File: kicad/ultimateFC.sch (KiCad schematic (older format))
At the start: 195 parts, among them J1 USB_B_Micro, J2 10132797-011100LF, J3 10132797-011100LF, J4 10132797-011100LF, J5 10132797-011100LF, J6 10132797-011100LF, Q1 DMP2066LSN-7, U1 EFM8BB21F16G-C-QFN20R, U10 NCP81253MNTBG, U11 SiZ200DT, U12 NCP81253MNTBG, U13 SiZ200DT, U14 TPS62824ADMQ, U15 SiZ200DT, U16 NCP81253MNTBG, U17 NCP81253MNTBG, U18 NCP81253MNTBG, U19 NCP81253MNTBG, U2 EFM8BB21F16G-C-QFN20R, U20 SiZ200DT, U21 SiZ200DT, U22 SiZ200DT, U23 SiZ200DT, U24 EFM8BB21F16G-C-QFN20R, U25 NCP81253MNTBG, U26 SiZ200DT, U27 NCP81253MNTBG, U28 NCP81253MNTBG, U29 SiZ200DT, U3 NCP81253MNTBG, U30 SiZ200DT, U31 INA186, U32 LMR33630CQRNX, U33 STM32F745VGHx, U34 AB7456, U35 ZOE-M8Q_ZOE-M8Q, U36 ICM-20602, U37 S25FL064L, U39 BMP280, U4 SiZ200DT, U5 TPS630701, U6 EFM8BB21F16G-C-QFN20R, U7 NCP81253MNTBG, U8 SiZ200DT, U9 NCP81253MNTBG, X1 Molex_734120110, Y1 CSTNE8M00G550000R0, Y2 ECS-270-8-47Q-CES-TR

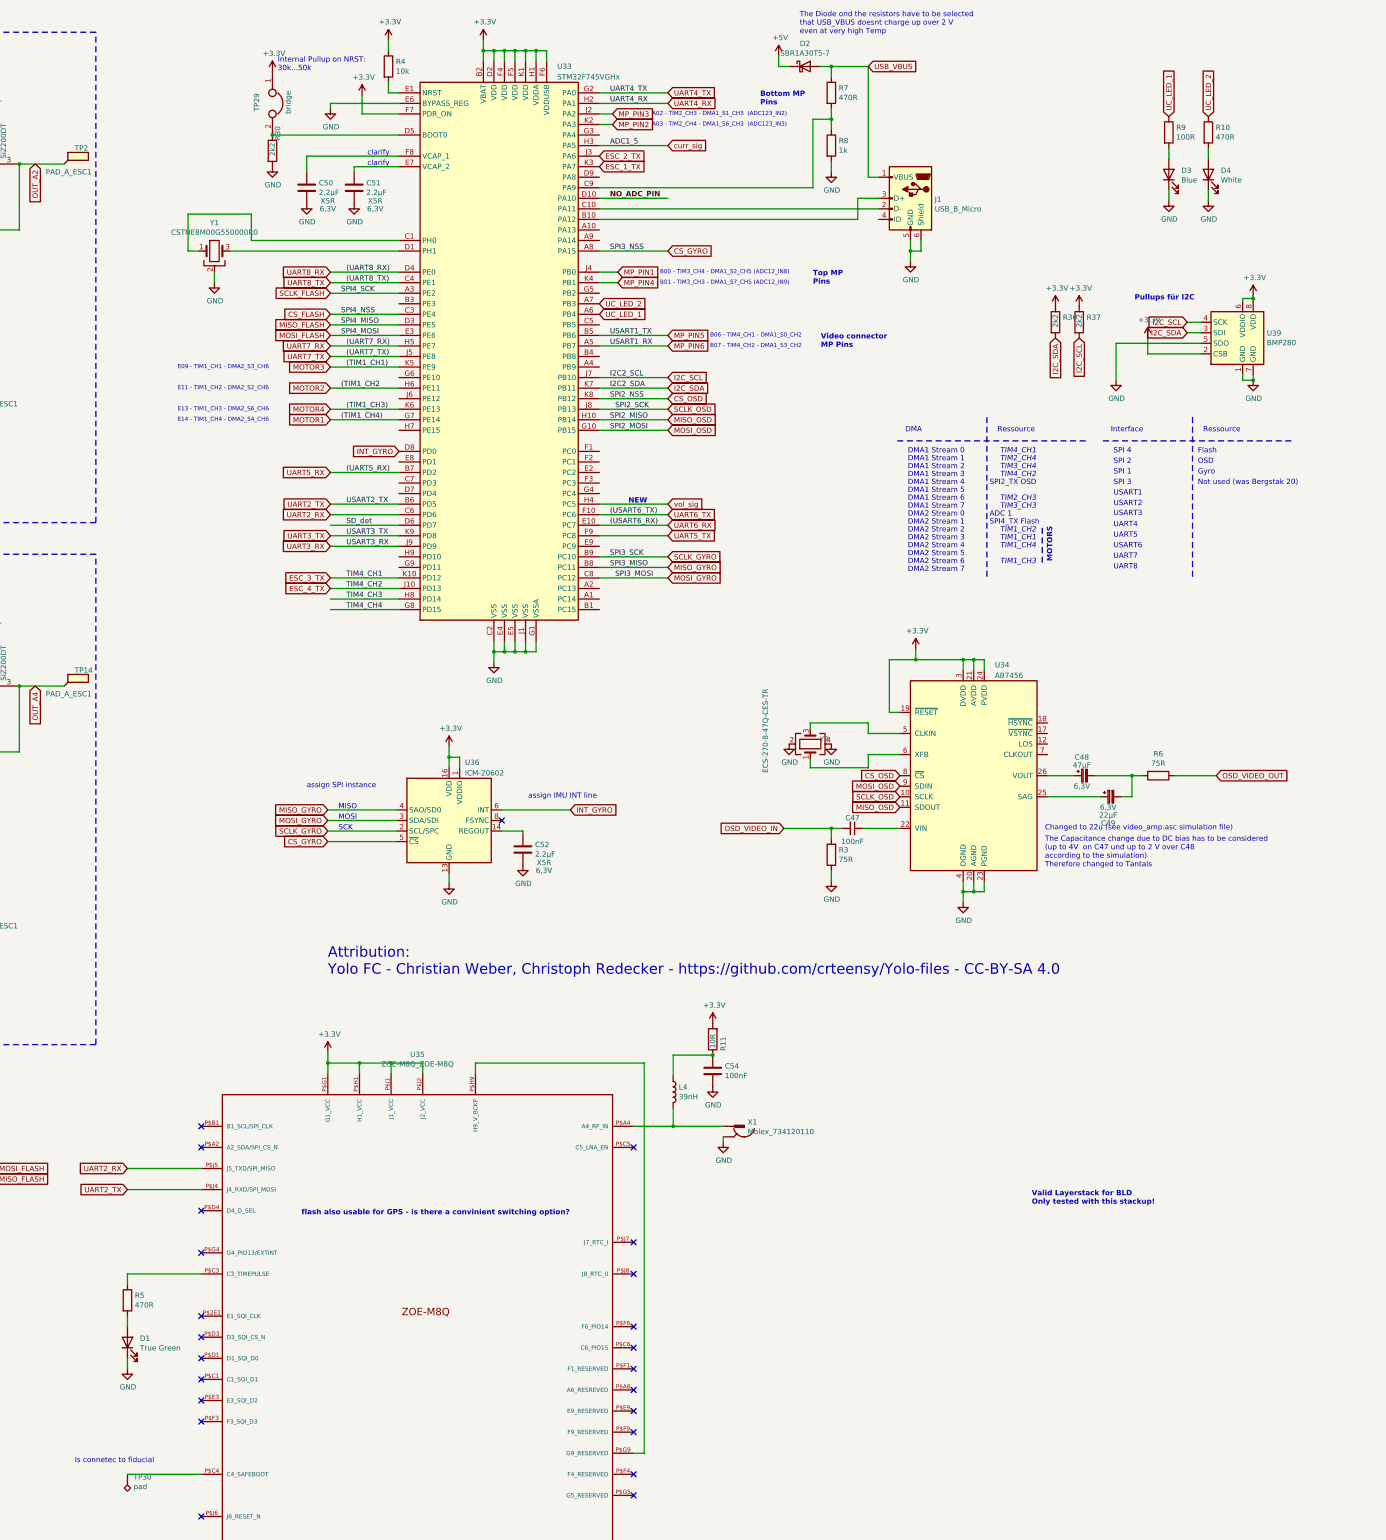
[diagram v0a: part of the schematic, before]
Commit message: exported gerbers and p+p files, started whoop mount adapter
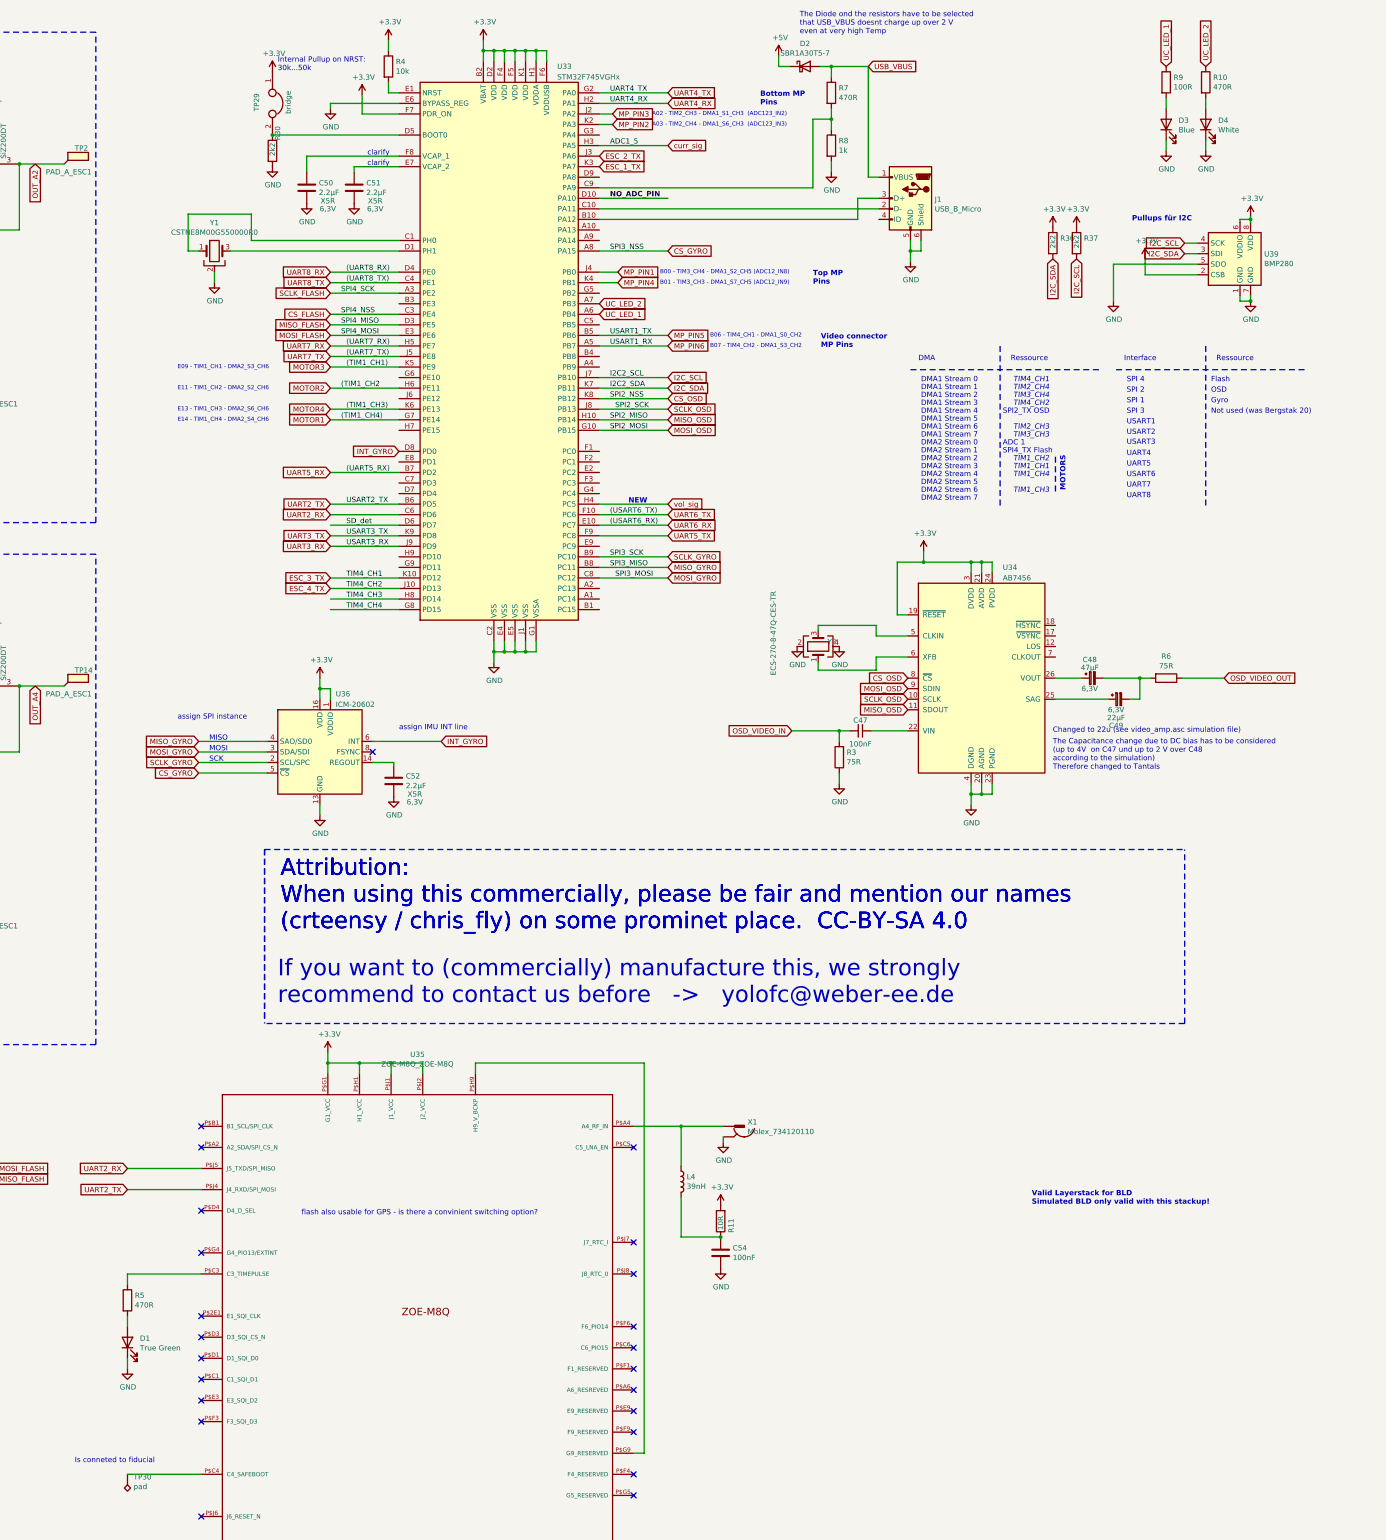
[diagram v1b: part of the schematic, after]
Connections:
- net at U35.P$A4 (A4_RF_IN), X1.1: now also L4.1; no longer L4.2
- net at C54.1, R11.1: now also L4.2; no longer L4.1
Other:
- note added: "Attribution:\nWhen using this commercially, please be fair and mention our names \n(crteensy / chris_fly) on some prominet place. CC-BY-SA 4.0"
- note added: "If you want to (commercially) manufacture this, we strongly \nrecommend to contact us before -> yolofc@weber-ee.de"
- note added: "Is conneted to fiducial"
- note added: "Valid Layerstack for BLD\nSimulated BLD only valid with this stackup!"
- note removed: "Attribution:\nYolo FC - Christian Weber, Christoph Redecker - https://github.com/crteensy/Yolo-files - CC-BY-SA 4.0"
- note removed: "Is connetec to fiducial"
- note removed: "Valid Layerstack for BLD\nOnly tested with this stackup!"
- moved on the sheet: C47, C48, C49, C52, C54, D3, D4, L4, R10, R11, R3, R36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

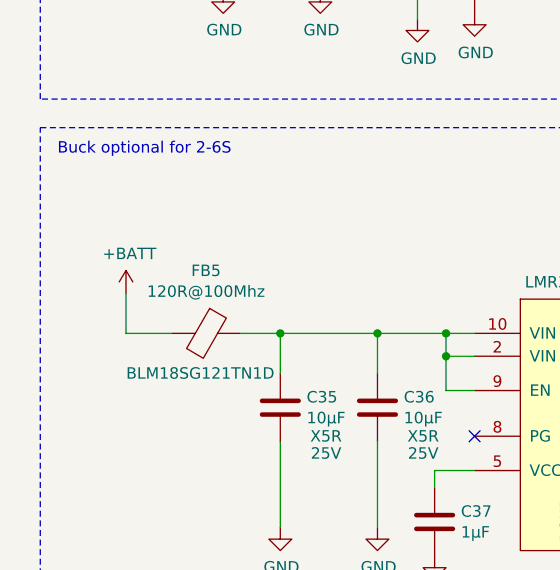
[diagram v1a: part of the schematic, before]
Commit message: added diode on 5V DCDC input
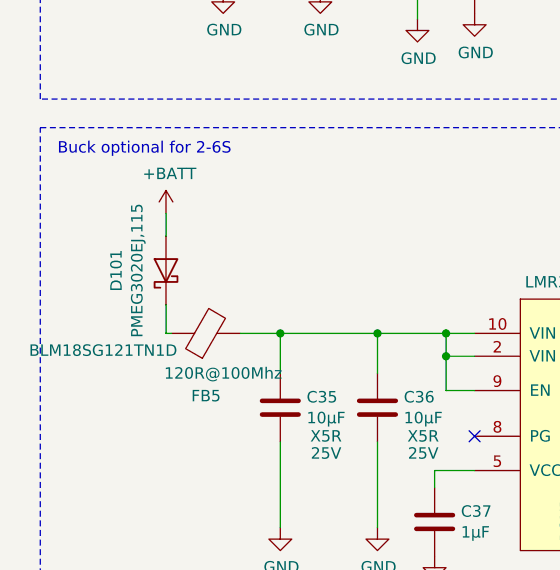
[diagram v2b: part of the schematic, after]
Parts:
- added D101: PMEG3020EJ,115, Diode_SMD:D_SOD-323, symbol Device:D_Schottky
- C28, C3, C33, C38, C47, C53, C54: footprint Capacitor_SMD:C_0201_0603Metric -> ultimateFC:C_0201_0603Metric_mod
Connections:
- net +BATT: now also D101.2 (A); no longer FB5.2
- net at C35.1, C36.1, U32.10 (VIN)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: now also FB5.2; no longer FB5.1
- new net: D101.1 (K), FB5.1
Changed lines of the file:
@@
 F 0 "C28" H 11315 12196 50  0000 L CNN
 F 1 "100nF" H 11315 12105 50  0000 L CNN
-F 2 "Capacitor_SMD:C_0201_0603Metric" H 11238 12000 50  0001 C CNN
+F 2 "ultimateFC:C_0201_0603Metric_mod" H 11238 12000 50  0001 C CNN
 F 3 "~" H 11200 12150 50  0001 C CNN
 F 4 "X5R" H 11200 12150 50  0001 C CNN "Dielektrikum"
@@
 F 0 "C33" H 14215 12271 50  0000 L CNN
 F 1 "100nF" H 14215 12180 50  0000 L CNN
-F 2 "Capacitor_SMD:C_0201_0603Metric" H 14138 12075 50  0001 C CNN
+F 2 "ultimateFC:C_0201_0603Metric_mod" H 14138 12075 50  0001 C CNN
 F 3 "~" H 14100 12225 50  0001 C CNN
 F 4 "X5R" H 14100 12225 50  0001 C CNN "Dielektrikum"
@@
 P 1625 14200
 F 0 "FB5" V 1351 14200 50  0000 C CNN
-F 1 "120R@100Mhz" V 1442 14200 50  0000 C CNN
+F 1 "120R@100Mhz" V 1450 14125 50  0000 C CNN
 F 2 "Inductor_SMD:L_0603_1608Metric" V 1555 14200 50  0001 C CNN
 F 3 "~" H 1625 14200 50  0001 C CNN
-F 4 "BLM18SG121TN1D" V 1800 14175 50  0000 C CNN "Mfr.No:"
+F 4 "BLM18SG121TN1D" V 1550 14650 50  0000 C CNN "Mfr.No:"
 F 5 "0,064" H 1625 14200 50  0001 C CNN "price@100[€]"
 F 6 "0,043" H 1625 14200 50  0001 C CNN "price@10[€]"
 F 7 "0,039" H 1625 14200 50  0001 C CNN "price@1k[€]"
 	1    1625 14200
-	0    1    1    0
+	0    -1   -1   0
 $EndComp
 Wire Wire Line
@@
 L power:+BATT #PWR0278
 U 1 1 5EE16FA9
-P 1275 14025
-F 0 "#PWR0278" H 1275 13875 50  0001 C CNN
-F 1 "+BATT" H 1290 14198 50  0000 C CNN
-F 2 "" H 1275 14025 50  0001 C CNN
-F 3 "" H 1275 14025 50  0001 C CNN
-	1    1275 14025
+P 1450 13675
+F 0 "#PWR0278" H 1450 13525 50  0001 C CNN
+F 1 "+BATT" H 1465 13848 50  0000 C CNN
+F 2 "" H 1450 13675 50  0001 C CNN
+F 3 "" H 1450 13675 50  0001 C CNN
+	1    1450 13675
 	1    0    0    -1
 $EndComp
-Wire Wire Line
-	1275 14025 1275 14200
-Wire Wire Line
-	1275 14200 1475 14200
 Wire Notes Line
 	900  13300 6225 13300
@@
 F 0 "C38" H 4090 14396 50  0000 L CNN
 F 1 "100nF" H 4090 14305 50  0000 L CNN
-F 2 "Capacitor_SMD:C_0201_0603Metric" H 4013 14200 50  0001 C CNN
+F 2 "ultimateFC:C_0201_0603Metric_mod" H 4013 14200 50  0001 C CNN
 F 3 "~" H 3975 14350 50  0001 C CNN
 F 4 "X5R" H 3975 14350 50  0001 C CNN "Dielektrikum"
@@
 F 0 "C47" V 26425 7475 50  0000 C CNN
 F 1 "100nF" V 26650 7475 50  0000 C CNN
-F 2 "Capacitor_SMD:C_0201_0603Metric" H 26525 7475 50  0001 C CNN
+F 2 "ultimateFC:C_0201_0603Metric_mod" H 26525 7475 50  0001 C CNN
 F 3 "~" H 26525 7475 50  0001 C CNN
 F 4 "X5R" H 26525 7475 50  0001 C CNN "Dielektrikum"
@@
 F 0 "C54" H 25315 12471 50  0000 L CNN
 F 1 "100nF" H 25315 12380 50  0000 L CNN
-F 2 "Capacitor_SMD:C_0201_0603Metric" H 25238 12275 50  0001 C CNN
+F 2 "ultimateFC:C_0201_0603Metric_mod" H 25238 12275 50  0001 C CNN
 F 3 "~" H 25200 12425 50  0001 C CNN
 F 4 "X5R" H 25200 12425 50  0001 C CNN "Dielektrikum"
@@
 F 0 "C3" H 2915 12696 50  0000 L CNN
 F 1 "100nF" H 2915 12605 50  0000 L CNN
-F 2 "Capacitor_SMD:C_0201_0603Metric" H 2838 12500 50  0001 C CNN
+F 2 "ultimateFC:C_0201_0603Metric_mod" H 2838 12500 50  0001 C CNN
 F 3 "~" H 2800 12650 50  0001 C CNN
 F 4 "X5R" H 2800 12650 50  0001 C CNN "Dielektrikum"
@@
 F 0 "C53" H 10415 14646 50  0000 L CNN
 F 1 "120pF" H 10415 14555 50  0000 L CNN
-F 2 "Capacitor_SMD:C_0201_0603Metric" H 10338 14450 50  0001 C CNN
+F 2 "ultimateFC:C_0201_0603Metric_mod" H 10338 14450 50  0001 C CNN
 F 3 "~" H 10300 14600 50  0001 C CNN
 F 4 "NP0" H 10300 14600 50  0001 C CNN "Dielektrikum"
@@
 Text Notes 21000 10075 0    157  ~ 0
 If you want to (commercially) manufacture this, we strongly \nrecommend to contact us before   ->   yolofc@weber-ee.de
+$Comp
+L Device:D_Schottky D?
+U 1 1 60AD2E6E
+P 1450 13925
+AR Path="/5ED1D96B/60AD2E6E" Ref="D?"  Part="1"
+AR Path="/60AD2E6E" Ref="D101"  Part="1"
+F 0 "D101" H 1450 14142 50  0000 C CNN
+F 1 "PMEG3020EJ,115" H 1450 14051 50  0000 C CNN
+F 2 "Diode_SMD:D_SOD-323" H 1450 13925 50  0001 C CNN
+F 3 "~" H 1450 13925 50  0001 C CNN
+F 4 "" H 1450 13925 50  0001 C CNN "Mfr.No:"
+F 5 "" H 1450 13925 50  0001 C CNN "price@100[€]"
+F 6 "" H 1450 13925 50  0001 C CNN "price@10[€]"
+F 7 "" H 1450 13925 50  0001 C CNN "price@1k[€]"
+	1    1450 13925
+	0    -1   -1   0
+$EndComp
+Wire Wire Line
+	1450 13675 1450 13775
+Wire Wire Line
+	1450 14075 1450 14200
+Wire Wire Line
+	1450 14200 1475 14200
 $EndSCHEMATC

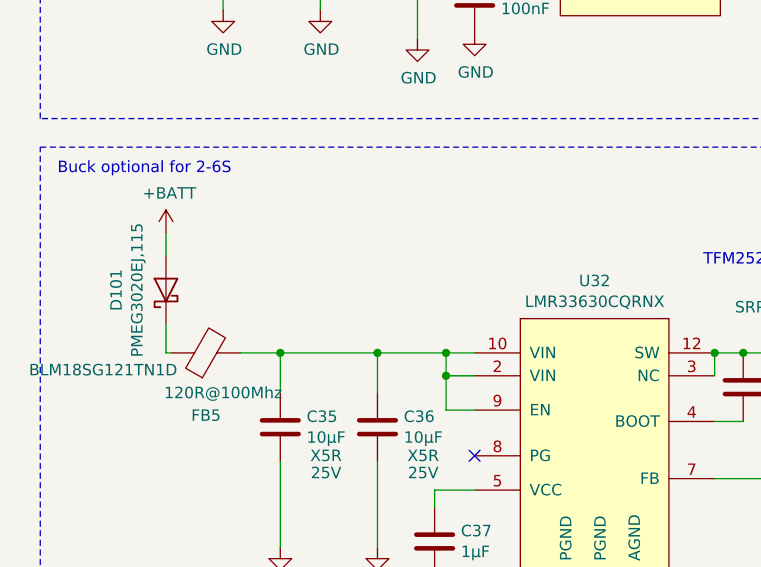
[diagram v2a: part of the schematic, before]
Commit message: added comment about diode alternative
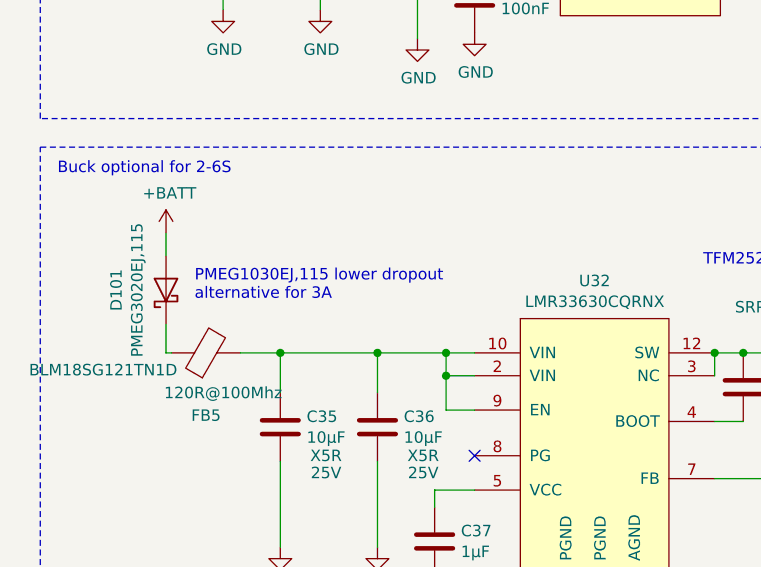
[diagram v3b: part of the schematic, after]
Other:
- note added: "PMEG1030EJ,115 lower dropout\nalternative for 3A"
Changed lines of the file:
@@
 Text Notes 21000 10075 0    157  ~ 0
 If you want to (commercially) manufacture this, we strongly \nrecommend to contact us before   ->   yolofc@weber-ee.de
+Wire Wire Line
+	1450 13675 1450 13775
+Wire Wire Line
+	1450 14075 1450 14200
+Wire Wire Line
+	1450 14200 1475 14200
 $Comp
 L Device:D_Schottky D?
@@
 	0    -1   -1   0
 $EndComp
-Wire Wire Line
-	1450 13675 1450 13775
-Wire Wire Line
-	1450 14075 1450 14200
-Wire Wire Line
-	1450 14200 1475 14200
+Text Notes 1575 13975 0    50   ~ 0
+PMEG1030EJ,115 lower dropout\nalternative for 3A
 $EndSCHEMATC

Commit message: some minor updates
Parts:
- C12, C13, C26, C27, C40, C5: symbol Device:CP -> ultimateFC-rescue:CP-Device
- C48, C49: symbol Device:CP_Small -> ultimateFC-rescue:CP_Small-Device
- FB1, FB2, FB3, FB4, FB5, FB6: symbol Device:Ferrite_Bead -> ultimateFC-rescue:Ferrite_Bead-Device
- TP23, TP29: symbol Device:Jumper -> ultimateFC-rescue:Jumper-Device
